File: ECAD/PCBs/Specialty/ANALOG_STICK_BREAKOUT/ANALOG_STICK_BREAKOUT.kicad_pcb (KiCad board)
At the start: 2 copper layers, 25 x 25 mm, 6 parts, among them J1 Conn_01x05

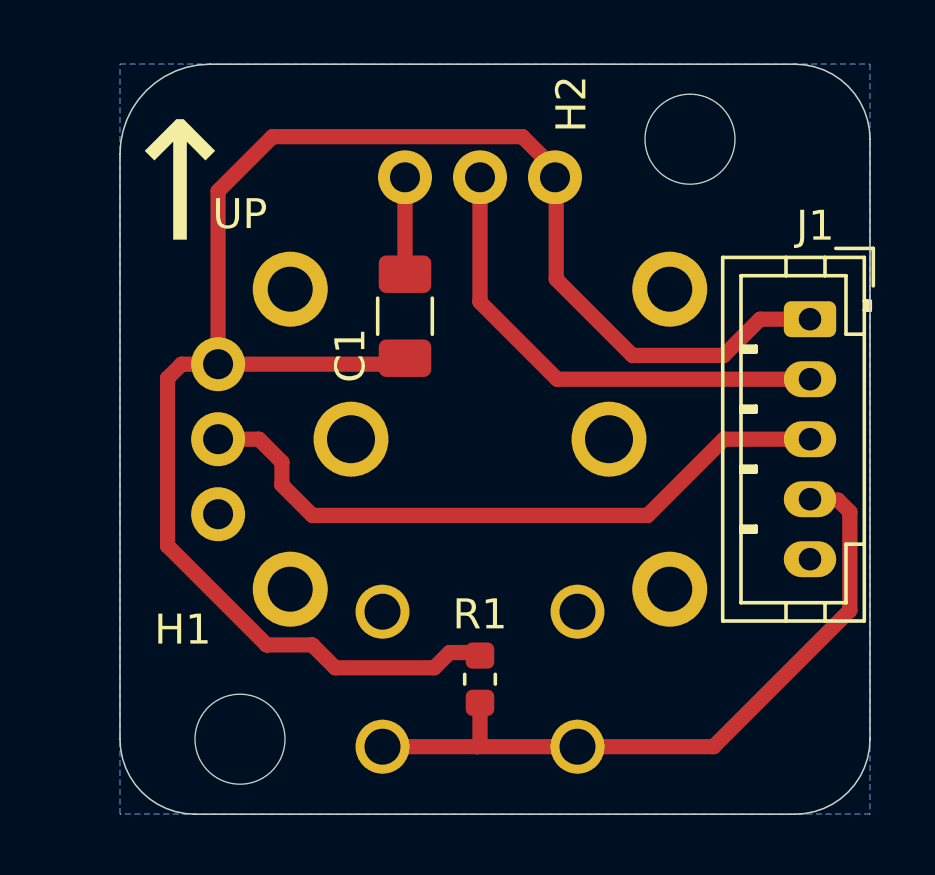
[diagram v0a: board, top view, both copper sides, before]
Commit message: Updated all the throttle components to use solder pads attached to the <switch> side components, and changed board shapes created new step models
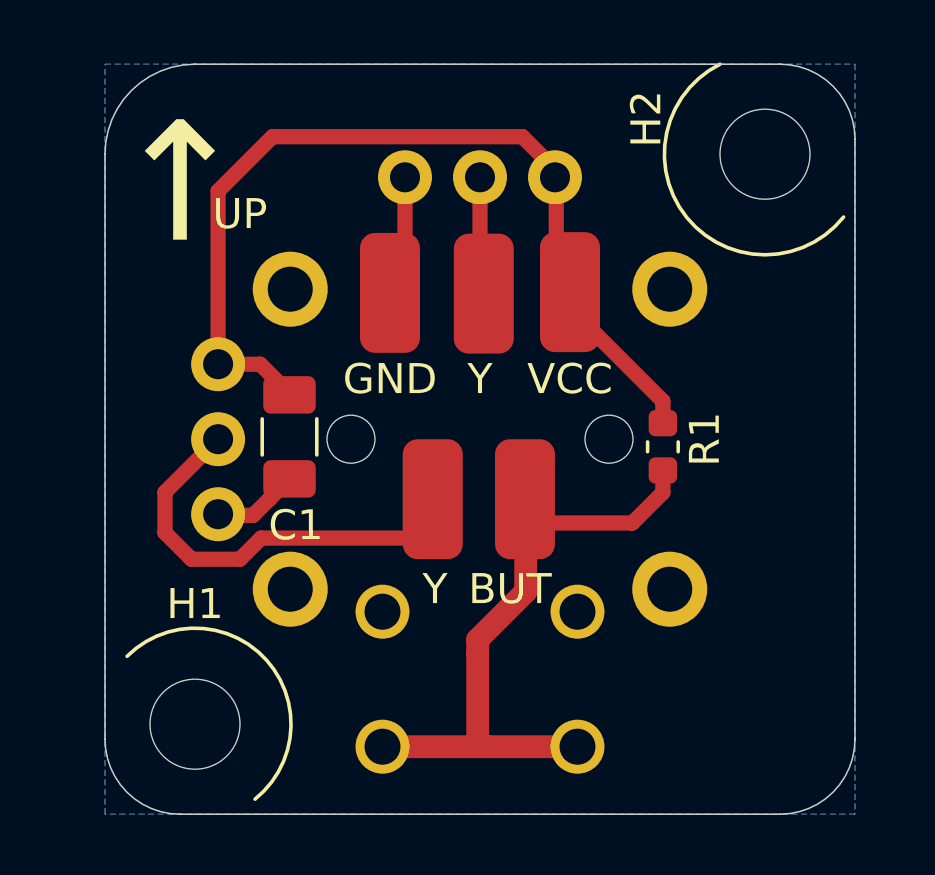
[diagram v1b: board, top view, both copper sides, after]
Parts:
- removed J1: Conn_01x05, Connector_JST:JST_PH_B5B-PH-K_1x05_P2.00mm_Vertical
- added J2: Conn_01x01, KiCAD_Libraries:SolderWirePad_1x01_SMD_2x4mm, F.Cu at (113.0, 80.1)
- added J3: Conn_01x01, KiCAD_Libraries:SolderWirePad_1x01_SMD_2x4mm, F.Cu at (110.1, 80.1)
- added J4: Conn_01x01, KiCAD_Libraries:SolderWirePad_1x01_SMD_2x4mm, F.Cu at (108.4, 87.0)
- added J5: Conn_01x01, KiCAD_Libraries:SolderWirePad_1x01_SMD_2x4mm, F.Cu at (111.5, 87.0)
- added J6: Conn_01x01, KiCAD_Libraries:SolderWirePad_1x01_SMD_2x4mm, F.Cu at (107.0, 80.1)
- moved R1 9.86 mm to (116.1, 85.3)
- moved C1 5.57 mm to (103.7, 84.9), turned to 270 degrees
- moved H2 2.55 mm to (119.5, 75.5)
- moved H1 1.58 mm to (100.5, 94.5)
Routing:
- net VCC: track 57.4 -> 29.1 mm
- net Net-(J3-Pad1): track 16.2 -> 4.01 mm
- net Net-(J4-Pad1): track 22.2 -> 13.1 mm
- net Net-(J5-Pad1): track 23.8 -> 20.0 mm
- net GND: track 3.23 -> 6.02 mm
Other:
- board text added: "BUT"
- board text added: "GND"
- board text added: "VCC"
- board text added: "Y"

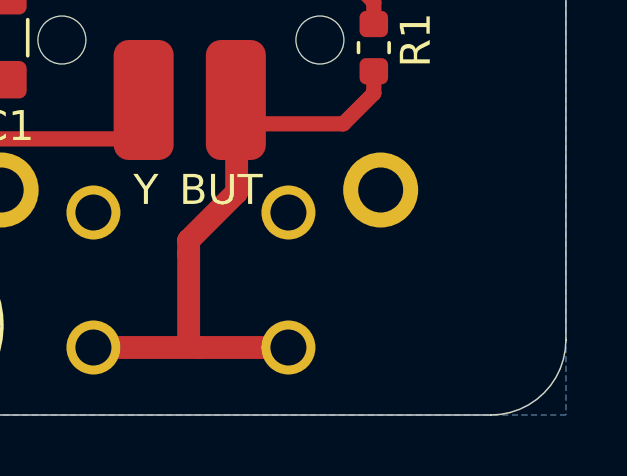
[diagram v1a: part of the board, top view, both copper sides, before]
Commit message: Added manufactuing files, and changed the 8 way hat to have screw holes on both sides from just one side.
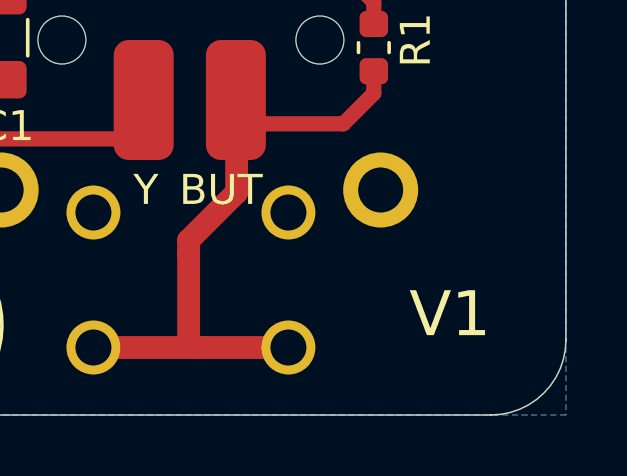
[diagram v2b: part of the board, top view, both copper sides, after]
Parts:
- added G***: LOGO, KiCAD_Libraries:OH_LOGO_NO_TEXT_11mm_5.9mm, B.Cu at (110.0, 82.0)
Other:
- board text added: "V1"
